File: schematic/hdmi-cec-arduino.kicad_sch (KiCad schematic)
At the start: 22 parts, among them J1 Power, J2 Digital/PWM, J3 Analog, J4 Digital/PWM, J5 HDMI_A, J6 HDMI_A, J7 Conn_01x03, J8 Conn_01x02, Q1 BC847, Q2 BC847

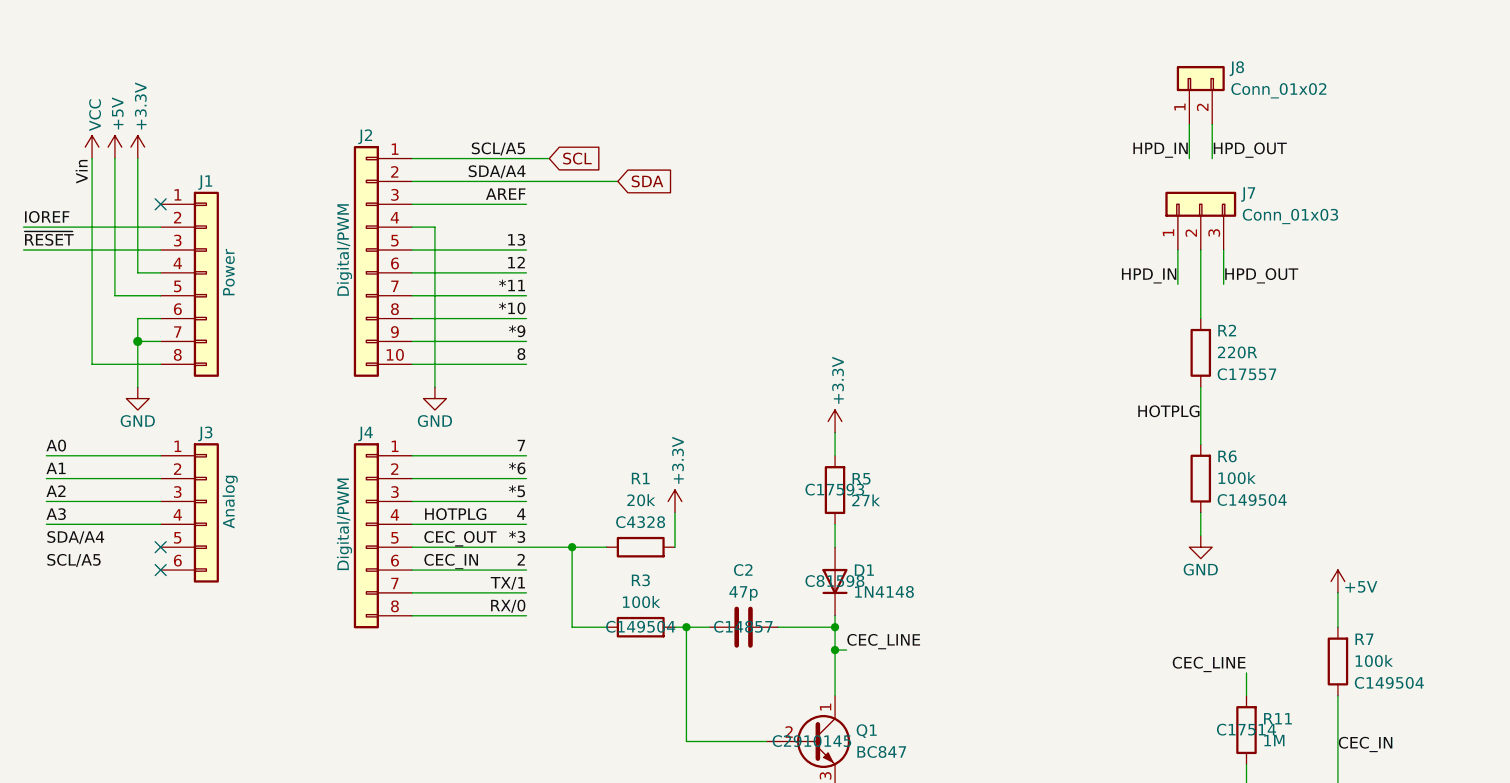
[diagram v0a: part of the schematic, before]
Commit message: Ready for production with Molex HDMI
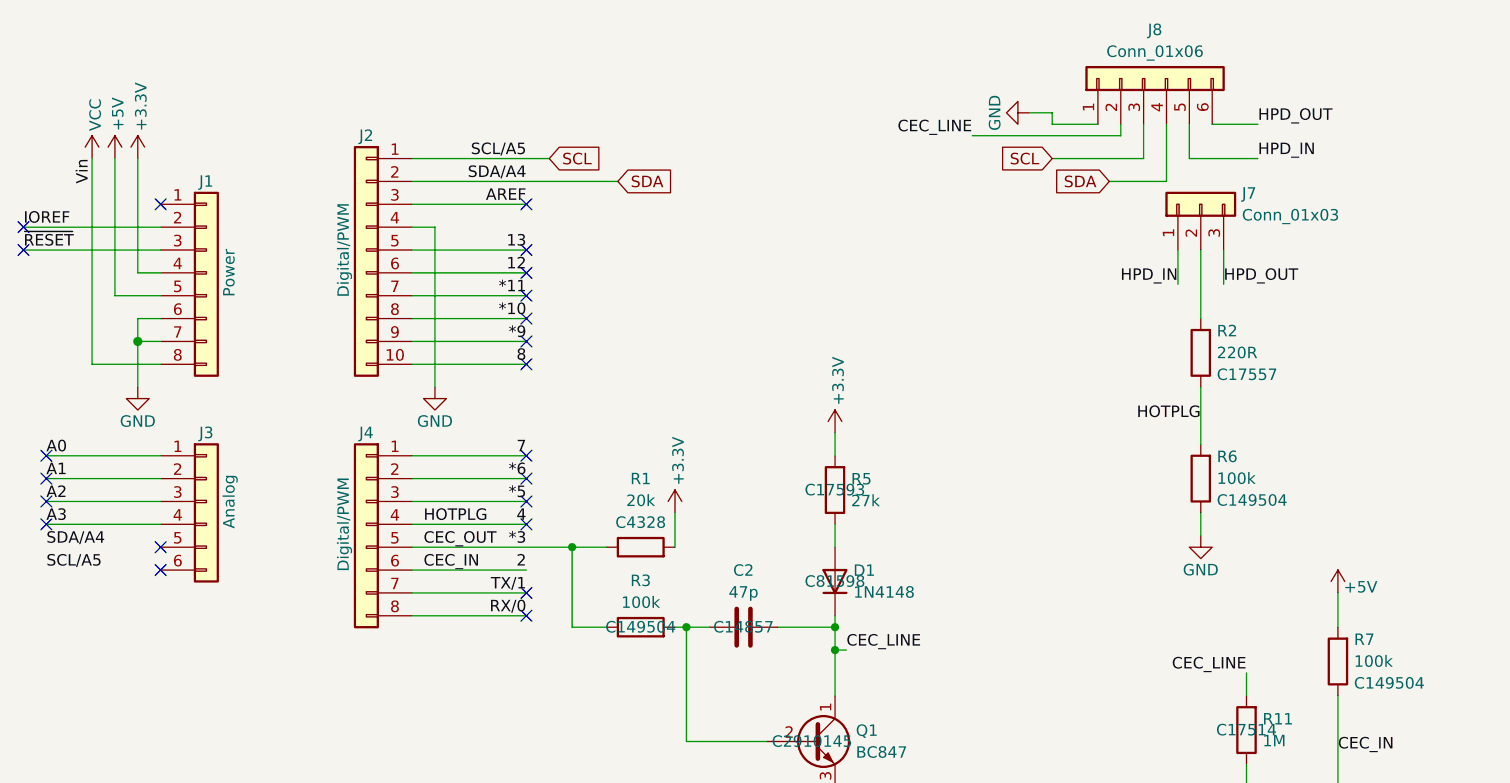
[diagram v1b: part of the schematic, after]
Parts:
- removed J8: Conn_01x02, Connector_PinHeader_2.54mm:PinHeader_1x02_P2.54mm_Vertical, symbol Connector_Generic:Conn_01x02
- added J8: Conn_01x06, Connector_PinHeader_2.54mm:PinHeader_1x06_P2.54mm_Vertical, symbol Connector_Generic:Conn_01x06
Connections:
- net CEC_LINE: now also J8.2 (Pin_2)
- net GND: now also J8.1 (Pin_1)
- net HPD_IN: now also J8.5 (Pin_5)
- net HPD_OUT: now also J8.6 (Pin_6)
- net SCL: now also J8.3 (Pin_3)
- net SDA: now also J8.4 (Pin_4)
- no-connect marks 4 -> 23

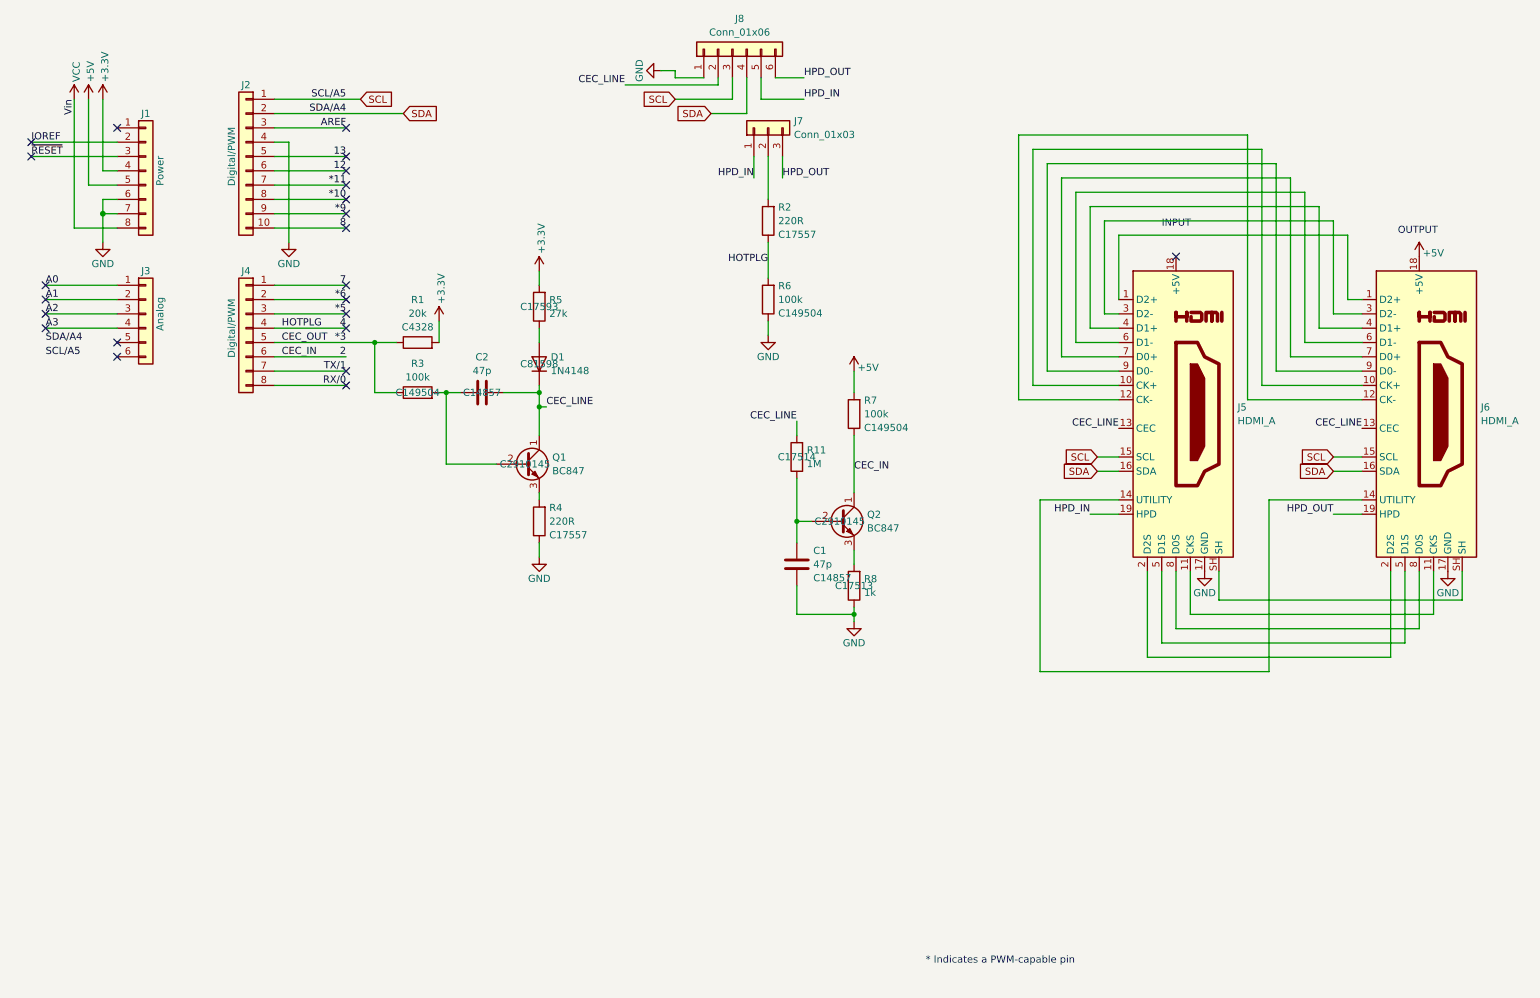
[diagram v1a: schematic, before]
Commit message: Re-Place HDMI connectors and add solder jumper for some signals
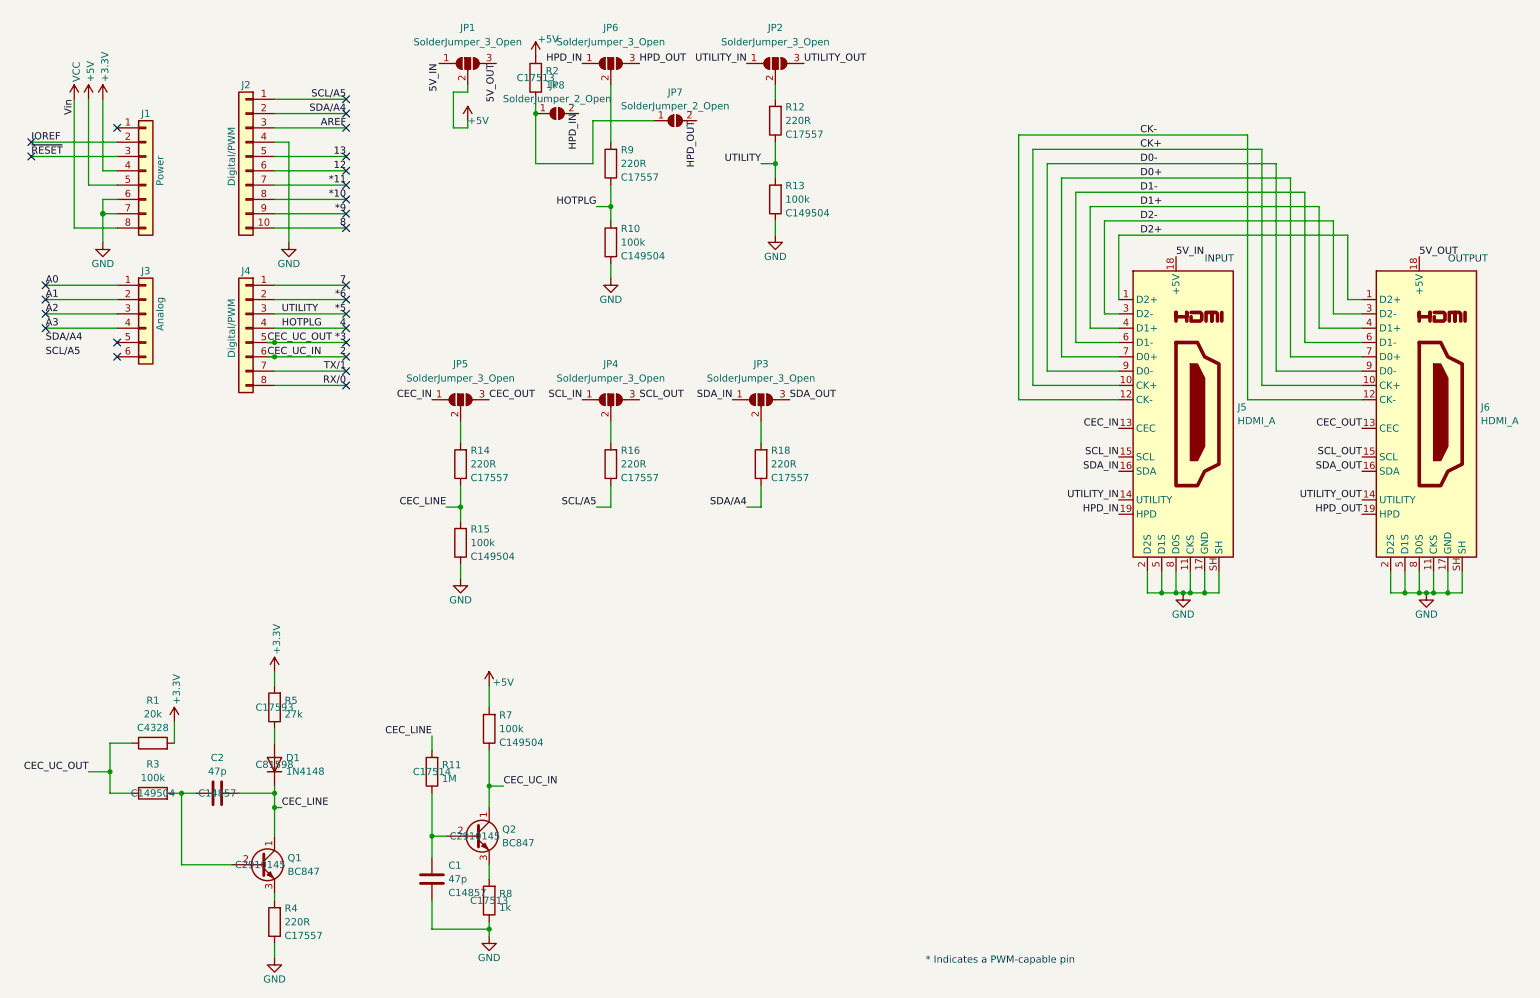
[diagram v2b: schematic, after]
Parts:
- removed J7: Conn_01x03, Connector_PinHeader_2.54mm:PinHeader_1x03_P2.54mm_Vertical, symbol Connector_Generic:Conn_01x03
- removed J8: Conn_01x06, Connector_PinHeader_2.54mm:PinHeader_1x06_P2.54mm_Vertical, symbol Connector_Generic:Conn_01x06
- removed R6: 100k, Resistor_SMD:R_0805_2012Metric, symbol Device:R
- added JP1, JP2, JP3, JP4, JP5, JP6: SolderJumper_3_Open, Jumper:SolderJumper-3_P2.0mm_Open_TrianglePad1.0x1.5mm, symbol Jumper:SolderJumper_3_Open
- added JP7, JP8: SolderJumper_2_Open, Jumper:SolderJumper-2_P1.3mm_Open_TrianglePad1.0x1.5mm, symbol Jumper:SolderJumper_2_Open
- added R10, R13, R15: 100k, Resistor_SMD:R_0805_2012Metric, symbol Device:R
- added R12, R14, R16, R18, R9: 220R, Resistor_SMD:R_0805_2012Metric, symbol Device:R
- J5, J6: footprint Connector_HDMI:HDMI_A_Molex_208658-1001_Horizontal -> Connector_HDMI:HDMI_A_Amphenol_10029449-x01xLF_Horizontal; LCSC C916313 -> C428493
- R2: value 220R -> 1k; LCSC C17557 -> C17513
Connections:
- net *5: now also R12.1, R13.2
- net +5V: now also R2.2, JP1.2 (C); no longer J6.18 (+5V)
- net 4: now also R10.2, R9.1; no longer R2.1
- net CEC_LINE: now also R14.1, R15.2; no longer J5.13 (CEC), J6.13 (CEC)
- net GND: now also J5.11 (CKS), J5.2 (D2S), J5.5 (D1S), J5.8 (D0S), J5.SH, J6.11 (CKS), J6.2 (D2S), J6.5 (D1S), J6.8 (D0S), J6.SH, R10.1, R13.1, R15.1
- net HPD_IN: now also JP6.1 (A), JP8.2 (B)
- net HPD_OUT: now also JP6.3 (B), JP7.2 (B)
- net D2+: now reaches J5.1 (D2+), J6.1 (D2+)
- net CK+: now reaches J5.10 (CK+), J6.10 (CK+)
- net CK-: now reaches J5.12 (CK-), J6.12 (CK-)
- net UTILITY_IN: now reaches J5.14 (UTILITY)
- net UTILITY_IN: now also JP2.1 (A); no longer J6.14 (UTILITY)
- net D2-: now reaches J5.3 (D2-), J6.3 (D2-)
- net D1+: now reaches J5.4 (D1+), J6.4 (D1+)
- net D1-: now reaches J5.6 (D1-), J6.6 (D1-)
- net D0+: now reaches J5.7 (D0+), J6.7 (D0+)
- net D0-: now reaches J5.9 (D0-), J6.9 (D0-)
- net 5V_IN: now reaches J5.18 (+5V)
- net 5V_IN: now also JP1.1 (A)
- removed net SCL: J2.1 (Pin_1), J5.15 (SCL), J6.15 (SCL)
- removed net SDA: J2.2 (Pin_2), J5.16 (SDA), J6.16 (SDA)
- new net: JP3.2 (C), R18.2
- new net: JP2.2 (C), R12.2
- new net: JP5.2 (C), R14.2
- new net: JP7.1 (A), JP8.1 (A), R2.1
- new net: JP6.2 (C), R9.2
- new net: JP4.2 (C), R16.2
- new net 5V_OUT: J6.18 (+5V), JP1.3 (B)
- new net CEC_IN: J5.13 (CEC), JP5.1 (A)
- new net CEC_OUT: J6.13 (CEC), JP5.3 (B)
- new net SCL_IN: J5.15 (SCL), JP4.1 (A)
- new net SCL_OUT: J6.15 (SCL), JP4.3 (B)
- new net SCL/A5: J2.1 (Pin_1), R16.1
- new net SDA_IN: J5.16 (SDA), JP3.1 (A)
- new net SDA_OUT: J6.16 (SDA), JP3.3 (B)
- new net SDA/A4: J2.2 (Pin_2), R18.1
- new net UTILITY_OUT: J6.14 (UTILITY), JP2.3 (B)
- no-connect marks 23 -> 26
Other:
- moved on the sheet: C1, C2, D1, Q1, Q2, R1, R11, R3, R4, R5, R7, R8
